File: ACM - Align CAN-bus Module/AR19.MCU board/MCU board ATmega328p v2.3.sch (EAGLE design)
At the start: 42 parts, among them IC1 ATMEGA328P-MMH, IC2 MIC5239-5.0YS_TR, IC3 MCP25625-E_ML, J1 AVR_SPI_PROG_3X2NS

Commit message: Finished .SCH v2.3
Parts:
- removed LED1: SML-A12DTT86, SML-A12DTT86:SML-A12DTT86
- removed P_CANH, P_CANL, P_GND, P_I/O1, P_I/O10, P_I/O11, P_I/O12, P_I/O2, P_I/O3, P_I/O4, P_I/O5, P_I/O6, P_I/O7, P_I/O8, P_I/O9, P_VCC: (no value), wirepad:2,15/1,0
- removed R3: 500Ohm, CRCW040295R3FKED(0402):CRCW040295R3FKED
- added 12V, I/O_AD0, I/O_AD1, I/O_AD2, I/O_AD3, I/O_AD4_SDA, I/O_AD5_SCL, I/O_D0_RX, I/O_D1_TX, I/O_D2_INT: (no value), wirepad:2,15/1,0
- added C13: 0.1uF, eagle-ltspice:CC0603
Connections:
- removed net DOTS.SDI: DOTSTAR.DIN, IC1.PD0_(RXD/PCINT16)
- removed net I/O1: IC1.PC0_(ADC0/PCINT8), P_I/O1.P
- removed net I/O10: IC1.(PCINT1/OC1A)_PB1, P_I/O10.P
- removed net I/O11: IC1.(PCINT19/OC2B/INT1)_PD3, P_I/O11.P
- removed net I/O12: IC1.(PCINT20/XCK/T0)_PD4, P_I/O12.P
- removed net I/O2: IC1.PC1_(ADC1/PCINT9), P_I/O2.P
- removed net I/O3: IC1.PC2_(ADC2/PCINT10), P_I/O3.P
- removed net I/O4: IC1.PC3_(ADC3/PCINT11), P_I/O4.P
- removed net I/O5: IC1.PC4_(ADC4/SDA/PCINT12), P_I/O5.P
- removed net I/O6: IC1.PC5_(ADC5/SCL/PCINT13), P_I/O9.P
- removed net I/O7: IC1.(PCINT21/OC0B/T1)_PD5, P_I/O8.P
- removed net I/O8: IC1.(PCINT22/OC0A/AIN0)_PD6, P_I/O7.P
- removed net I/O9: IC1.(PCINT23/AIN1)_PD7, P_I/O6.P
- removed net N$4: IC1.EP_-_GND
- removed net N$8: IC1.PD1_(TXD/PCINT17)
- removed net SS: IC1.(PCINT2/SS/OC1B)_PB2
- removed net VCC: F1.1, P_VCC.P
- new net CS_DOTS: DOTSTAR.DIN
- new net DOTS_CS: IC1.(PCINT0/CLKO/ICP1)_PB0
- new net I/O_AD0: I/O_AD0.P, IC1.PC0_(ADC0/PCINT8)
- new net I/O_AD1: I/O_AD1.P, IC1.PC1_(ADC1/PCINT9)
- new net I/O_AD2: I/O_AD2.P, IC1.PC2_(ADC2/PCINT10)
- new net I/O_AD3: I/O_AD3.P, IC1.PC3_(ADC3/PCINT11)
- new net I/O_AD4_SCL: I/O_AD4_SDA.P, IC1.PC4_(ADC4/SDA/PCINT12)
- new net I/O_AD5_SCL: I/O_AD5_SCL.P, IC1.PC5_(ADC5/SCL/PCINT13)
- new net I/O_D0_RX: I/O_D0_RX.P, IC1.PD0_(RXD/PCINT16)
- new net I/O_D1_TX: I/O_D1_TX.P, IC1.PD1_(TXD/PCINT17)
- new net I/O_D2_INT: I/O_D2_INT.P, IC1.(PCINT19/OC2B/INT1)_PD3
- net 5V: now also C13.1, IC1.AREF
- net CANH: no longer P_CANH.P
- net CANL: no longer P_CANL.P
- net CAN_CS: now also IC1.(PCINT1/OC1A)_PB1; no longer IC1.(PCINT0/CLKO/ICP1)_PB0
- net GND: now also C13.2, IC1.EP_-_GND, IC2.TAB; no longer LED1.A, P_GND.P
- net N$2: no longer R3.2
- net N$3: now also 12V.P, F1.1; no longer LED1.K, R3.1
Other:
- note added: "12V to 5V with fuse"
- note added: "16 MHz crystal for CAN IC"
- note added: "16 MHz crystal for MCU"
- note added: "CAN IC"
- note added: "ISP programming pins"
- note added: "MCU IC"
- note added: "Physical reset"
- moved on the sheet: C10, C11, C12, C2, C3, C4, C9, DOTSTAR, F1, IC1, J1, R1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

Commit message: Begynt å lage board
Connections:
- removed net CS_DOTS: DOTSTAR.DIN
- net CAN_MISO: now also IC1.(PCINT4/MISO)_PB4
- net CAN_MOSI: now also IC1.(PCINT3/OC2A/MOSI)_PB3
- net DOTS_CS: now also DOTSTAR.DIN
- net MISO: no longer IC1.(PCINT4/MISO)_PB4
- net MOSI: no longer IC1.(PCINT3/OC2A/MOSI)_PB3
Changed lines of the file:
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@@
 <label x="111.76" y="160.02" size="1.778" layer="95"/>
-</segment>
-<segment>
-<pinref part="IC1" gate="G$1" pin="(PCINT3/OC2A/MOSI)_PB3"/>
-<wire x1="88.9" y1="-55.88" x2="45.72" y2="-55.88" width="0.1524" layer="91"/>
-<wire x1="45.72" y1="-55.88" x2="45.72" y2="-43.18" width="0.1524" layer="91"/>
-<label x="88.9" y="-55.88" size="1.778" layer="95"/>
 </segment>
 </net>
@@
 <wire x1="76.2" y1="162.56" x2="76.2" y2="165.1" width="0.1524" layer="91"/>
 <wire x1="76.2" y1="165.1" x2="71.12" y2="165.1" width="0.1524" layer="91"/>
-</segment>
-<segment>
-<pinref part="IC1" gate="G$1" pin="(PCINT4/MISO)_PB4"/>
-<wire x1="48.26" y1="-43.18" x2="48.26" y2="-50.8" width="0.1524" layer="91"/>
-<wire x1="48.26" y1="-50.8" x2="88.9" y2="-50.8" width="0.1524" layer="91"/>
-<label x="88.9" y="-50.8" size="1.778" layer="95"/>
 </segment>
 </net>
@@
 <wire x1="203.2" y1="73.66" x2="198.12" y2="73.66" width="0.1524" layer="91"/>
 </segment>
+<segment>
+<pinref part="IC1" gate="G$1" pin="(PCINT4/MISO)_PB4"/>
+<wire x1="48.26" y1="-43.18" x2="48.26" y2="-50.8" width="0.1524" layer="91"/>
+<wire x1="48.26" y1="-50.8" x2="88.9" y2="-50.8" width="0.1524" layer="91"/>
+<label x="88.9" y="-50.8" size="1.778" layer="95"/>
+</segment>
 </net>
 <net name="CAN_MOSI" class="0">
@@
 <wire x1="205.74" y1="68.58" x2="205.74" y2="76.2" width="0.1524" layer="91"/>
 <wire x1="205.74" y1="76.2" x2="198.12" y2="76.2" width="0.1524" layer="91"/>
+</segment>
+<segment>
+<pinref part="IC1" gate="G$1" pin="(PCINT3/OC2A/MOSI)_PB3"/>
+<wire x1="88.9" y1="-55.88" x2="45.72" y2="-55.88" width="0.1524" layer="91"/>
+<wire x1="45.72" y1="-55.88" x2="45.72" y2="-43.18" width="0.1524" layer="91"/>
+<label x="88.9" y="-55.88" size="1.778" layer="95"/>
 </segment>
 </net>
@@
 <wire x1="205.74" y1="15.24" x2="190.5" y2="15.24" width="0.1524" layer="91"/>
 <wire x1="190.5" y1="40.64" x2="190.5" y2="15.24" width="0.1524" layer="91"/>
-</segment>
-</net>
-<net name="CS_DOTS" class="0">
-<segment>
-<pinref part="DOTSTAR" gate="G$1" pin="DIN"/>
-<wire x1="193.04" y1="-55.88" x2="185.42" y2="-55.88" width="0.1524" layer="91"/>
-<label x="172.72" y="-50.8" size="1.778" layer="95" rot="MR0"/>
-<wire x1="185.42" y1="-55.88" x2="185.42" y2="-50.8" width="0.1524" layer="91"/>
-<wire x1="185.42" y1="-50.8" x2="172.72" y2="-50.8" width="0.1524" layer="91"/>
 </segment>
 </net>
@@
 <label x="88.9" y="-66.04" size="1.778" layer="95"/>
 </segment>
-</net>
+<segment>
+<pinref part="DOTSTAR" gate="G$1" pin="DIN"/>
+<wire x1="193.04" y1="-55.88" x2="185.42" y2="-55.88" width="0.1524" layer="91"/>
+<label x="172.72" y="-50.8" size="1.778" layer="95" rot="MR0"/>
+<wire x1="185.42" y1="-55.88" x2="185.42" y2="-50.8" width="0.1524" layer="91"/>
+<wire x1="185.42" y1="-50.8" x2="172.72" y2="-50.8" width="0.1524" layer="91"/>
+</segment>
+</net>

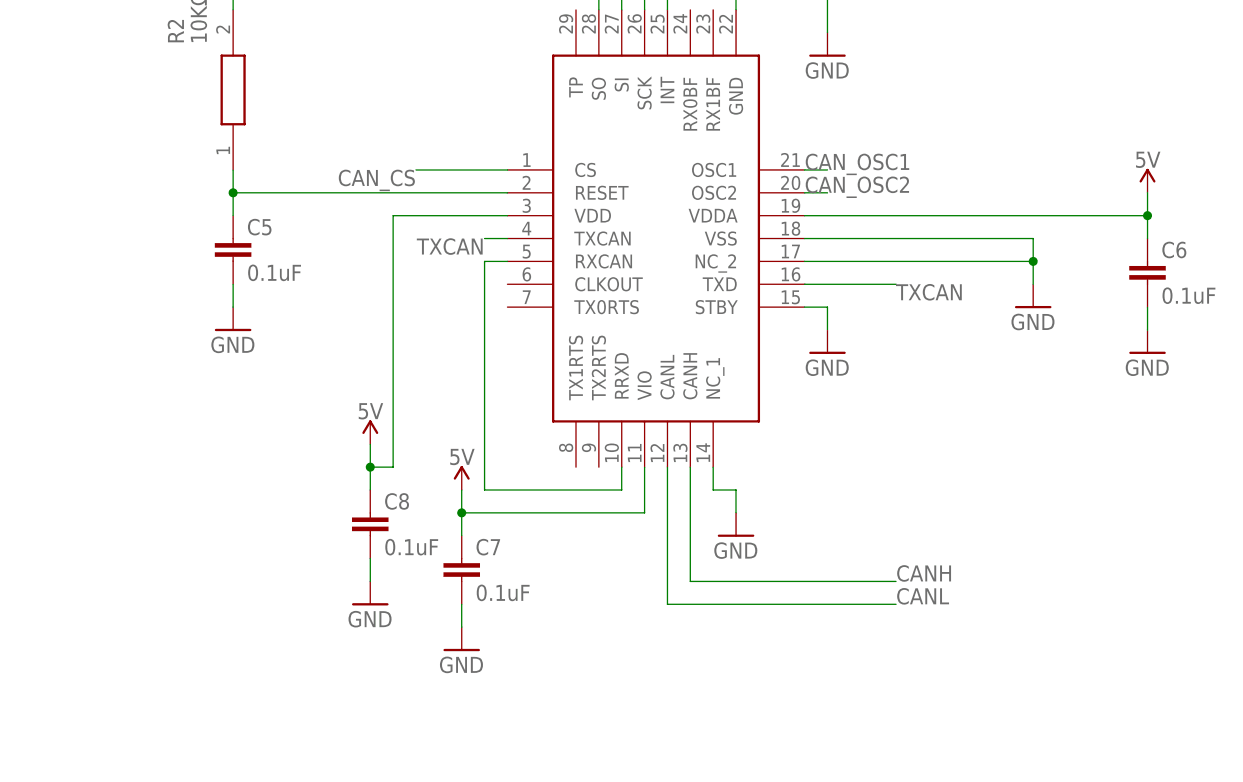
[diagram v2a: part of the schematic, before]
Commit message: Progress with tracing (40 Air-errors left), Change text size to 20
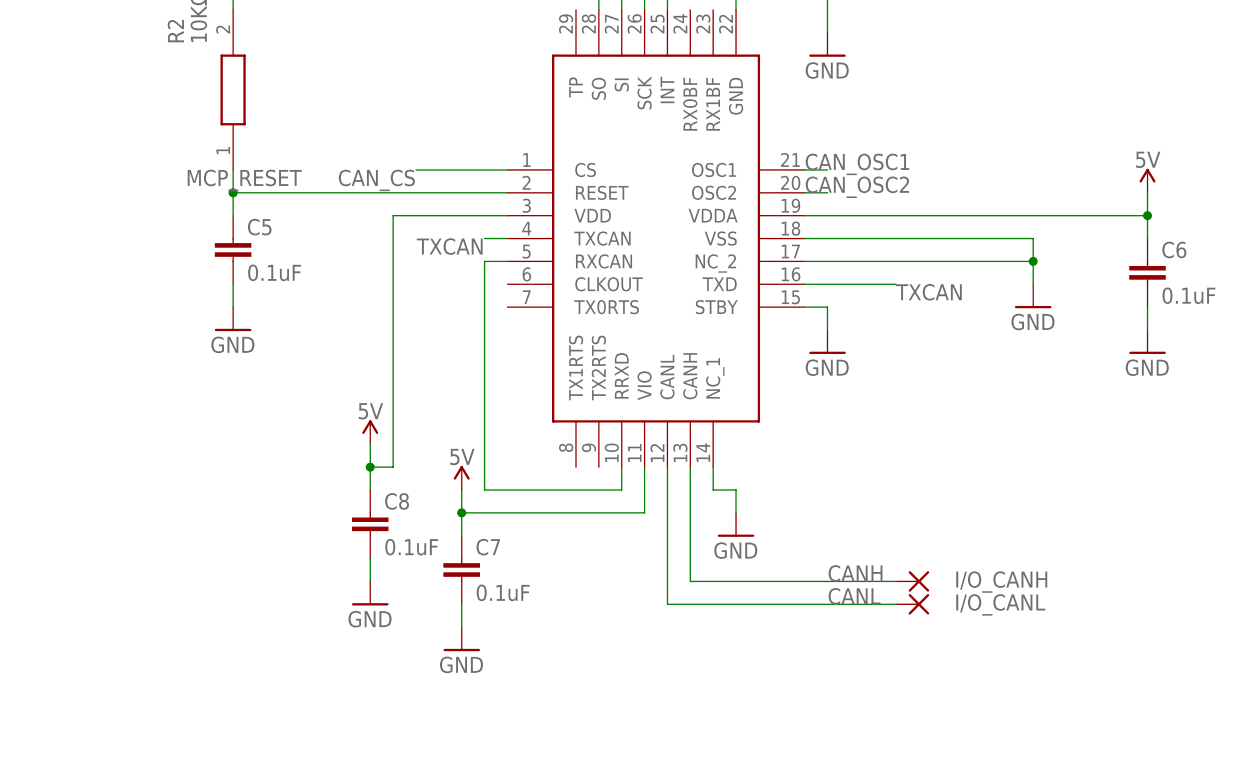
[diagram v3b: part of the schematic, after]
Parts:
- added I/O_CANH, I/O_CANL: (no value), wirepad:2,15/1,0
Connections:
- net N$1 renamed MCP_RESET
- net N$2 renamed 12V_FUSED
- net N$3 renamed 12V_UNFUSED
- net CANH: now also I/O_CANH.P
- net CANL: now also I/O_CANL.P

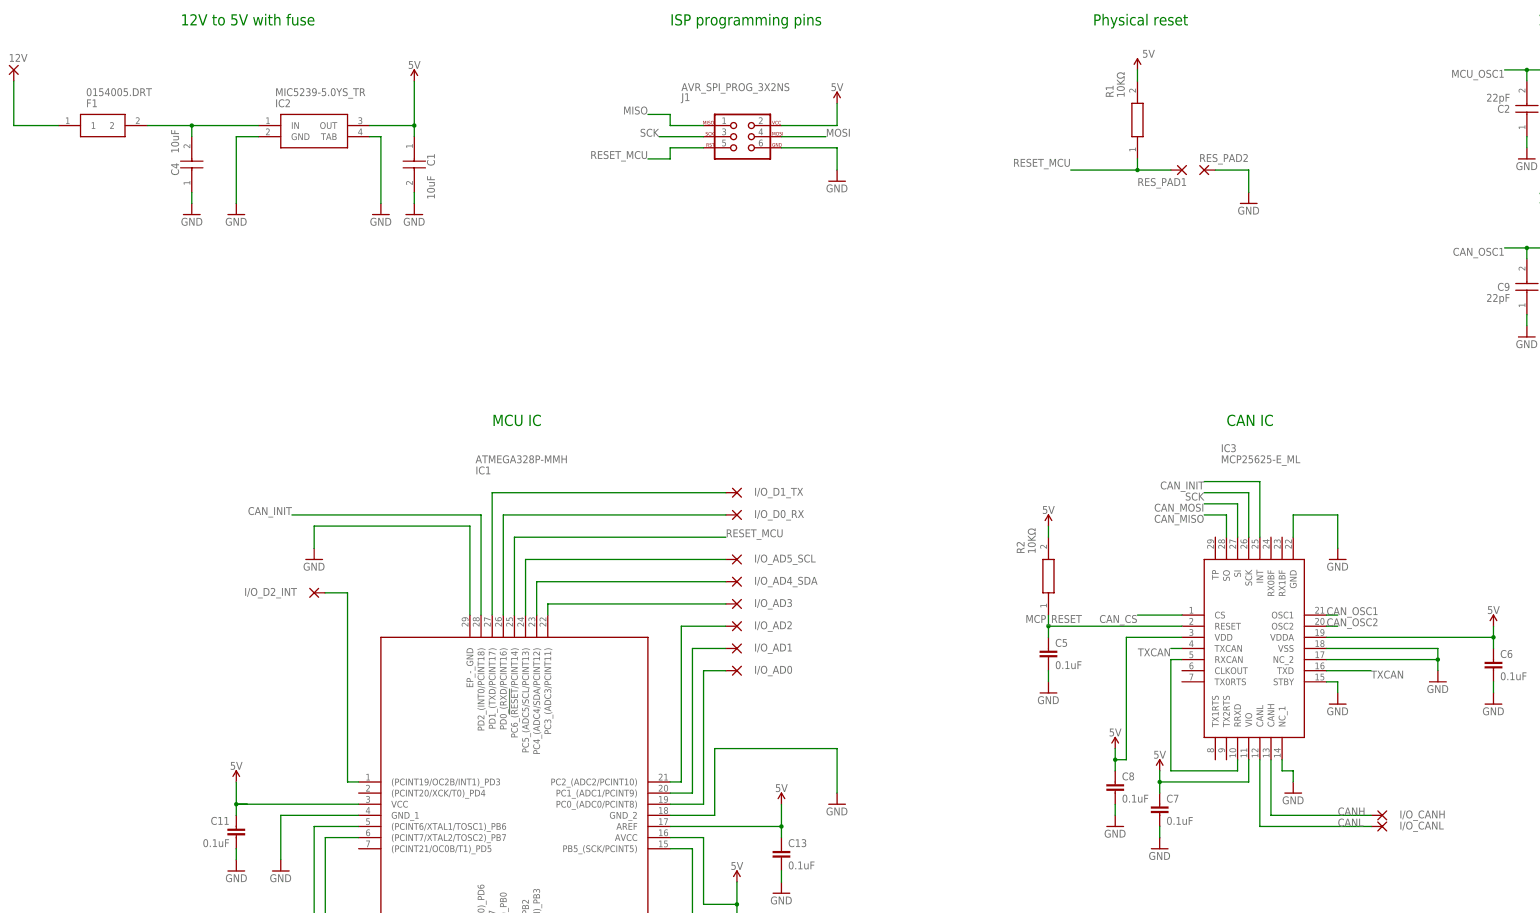
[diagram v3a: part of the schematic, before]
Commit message: ADDED: Support for Half cut/castellated holes.
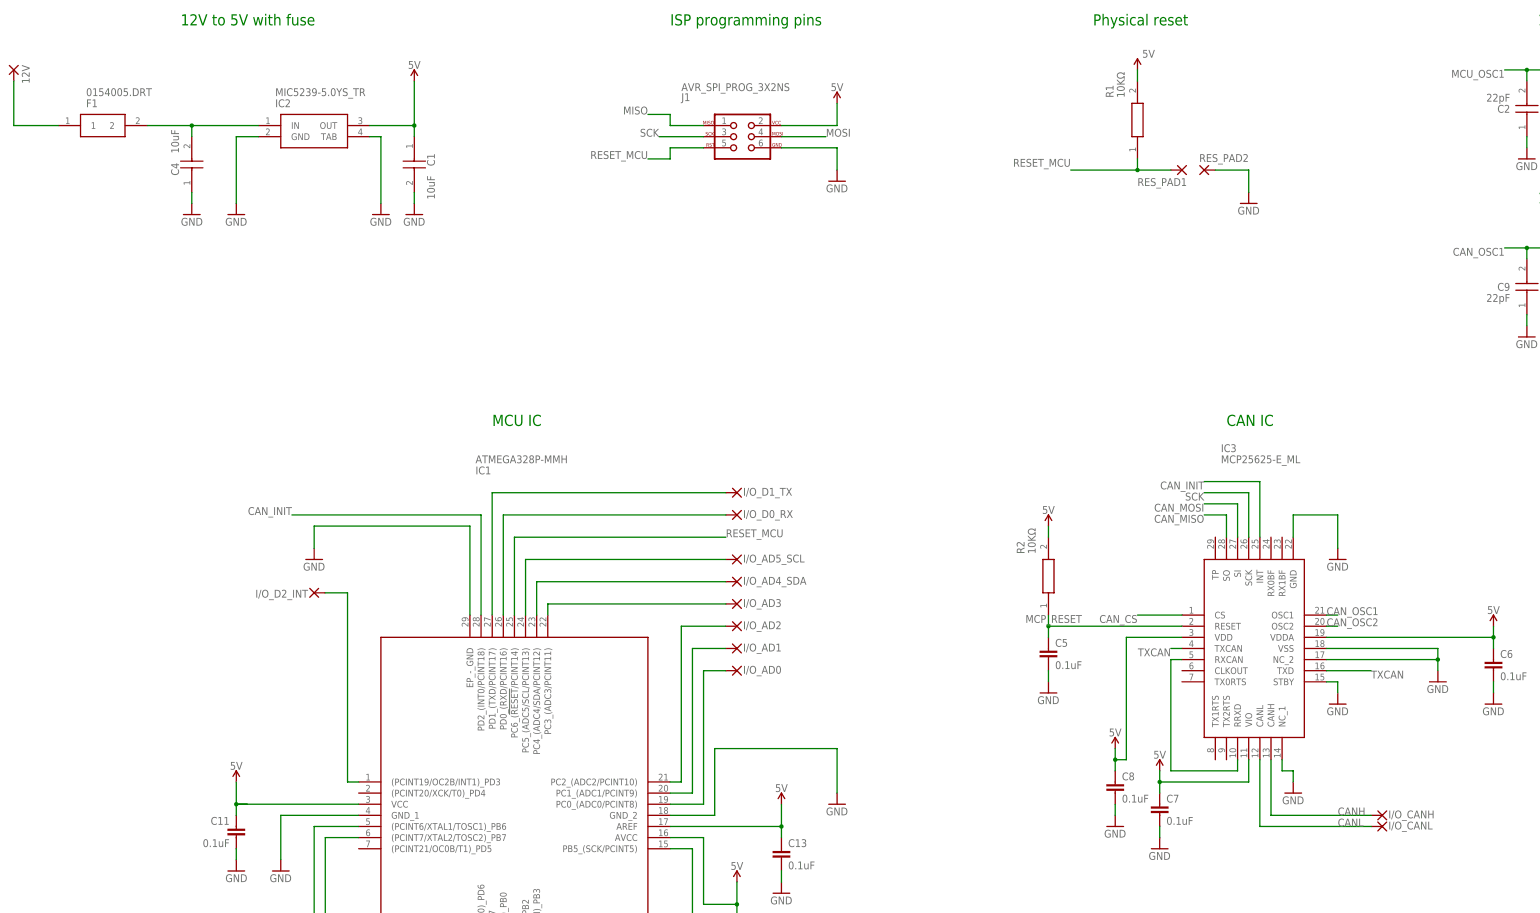
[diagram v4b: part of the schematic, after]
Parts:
- 12V, I/O_AD0, I/O_AD1, I/O_AD2, I/O_AD3, I/O_AD4_SDA, I/O_AD5_SCL, I/O_CANH, I/O_CANL, I/O_D0_RX, I/O_D1_TX, I/O_D2_INT: device wirepad:2,15/1,0 -> wirepad_edit:2,15/1,0(HALFHOLE)H+V
